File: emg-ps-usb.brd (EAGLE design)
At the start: 58.4 x 19.1 mm, 13 parts, among them U2 PHONE_JACK_MONO, X1 53047-04

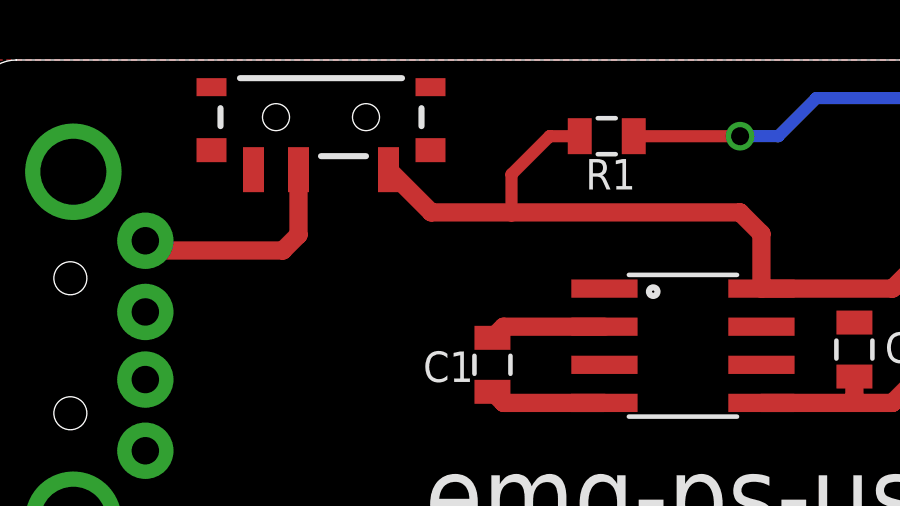
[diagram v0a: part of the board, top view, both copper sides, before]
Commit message: Cleaned up schematic and added a frame.
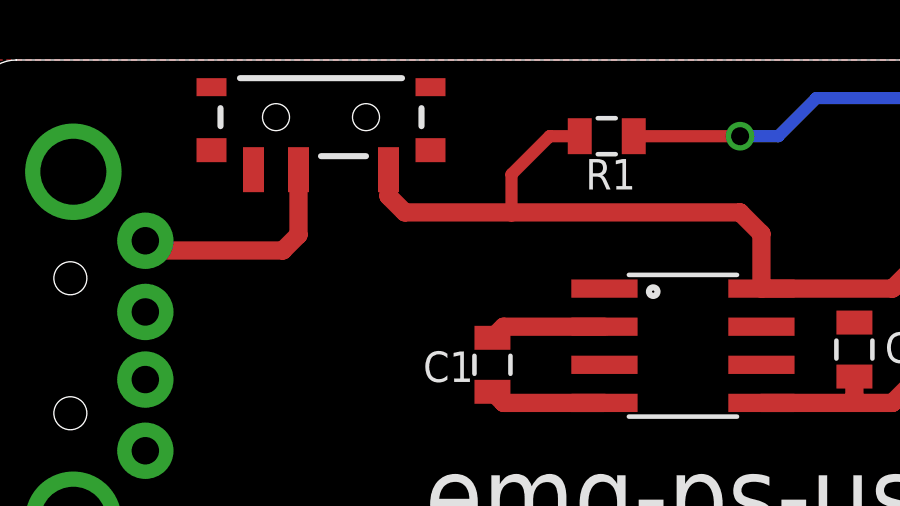
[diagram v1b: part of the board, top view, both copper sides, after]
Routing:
- net VBUS: track 33.2 -> 33.7 mm
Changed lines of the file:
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@@
 <wire x1="26.1112" y1="13.2588" x2="25.4" y2="13.97" width="0.6096" layer="1"/>
 <wire x1="25.4" y1="13.97" x2="17.78" y2="13.97" width="0.6096" layer="1"/>
-<wire x1="17.78" y1="13.97" x2="15.105" y2="13.97" width="0.6096" layer="1"/>
-<wire x1="15.105" y1="13.97" x2="13.68" y2="15.395" width="0.6096" layer="1"/>
 <wire x1="20.055" y1="16.51" x2="19.05" y2="16.51" width="0.4064" layer="1"/>
 <wire x1="19.05" y1="16.51" x2="17.78" y2="15.24" width="0.4064" layer="1"/>
 <wire x1="17.78" y1="15.24" x2="17.78" y2="13.97" width="0.4064" layer="1"/>
+<wire x1="13.68" y1="15.395" x2="13.68" y2="14.514" width="0.6096" layer="1"/>
+<wire x1="13.68" y1="14.514" x2="14.224" y2="13.97" width="0.6096" layer="1"/>
+<wire x1="14.224" y1="13.97" x2="17.78" y2="13.97" width="0.6096" layer="1"/>
 </signal>
 <signal name="N$3">

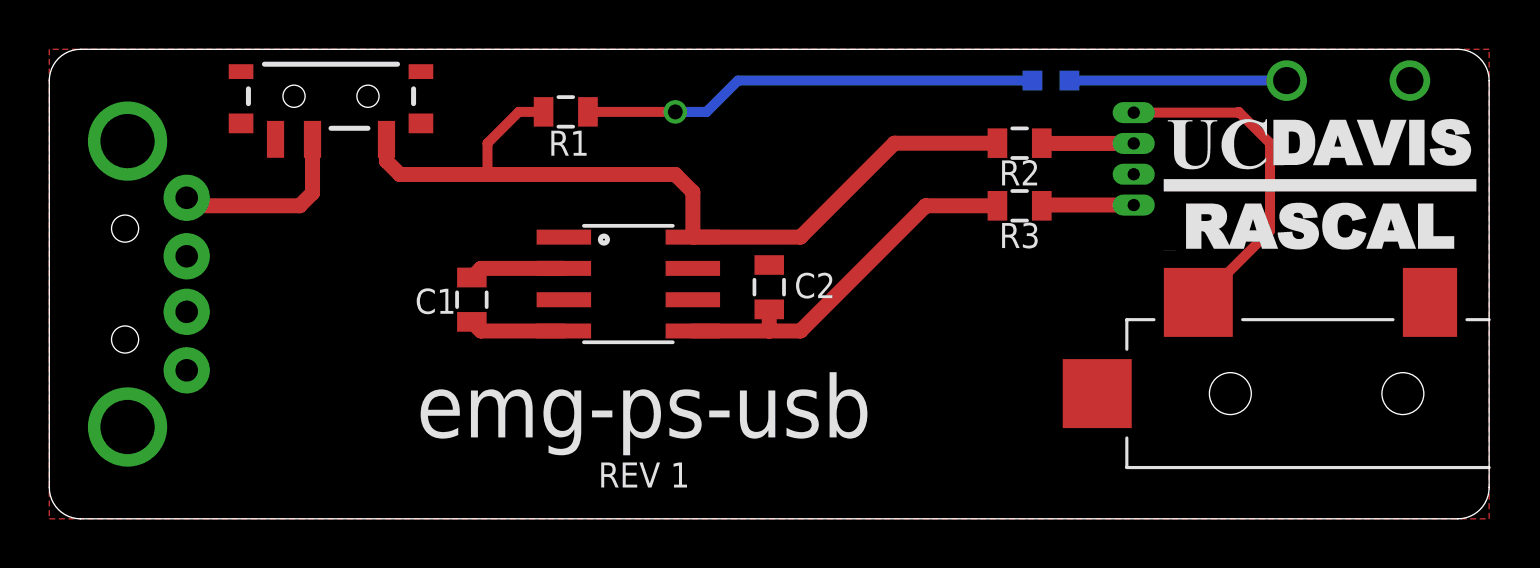
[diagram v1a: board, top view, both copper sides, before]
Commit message: Added labels to the EMG amp connector. Decreased size of component names.
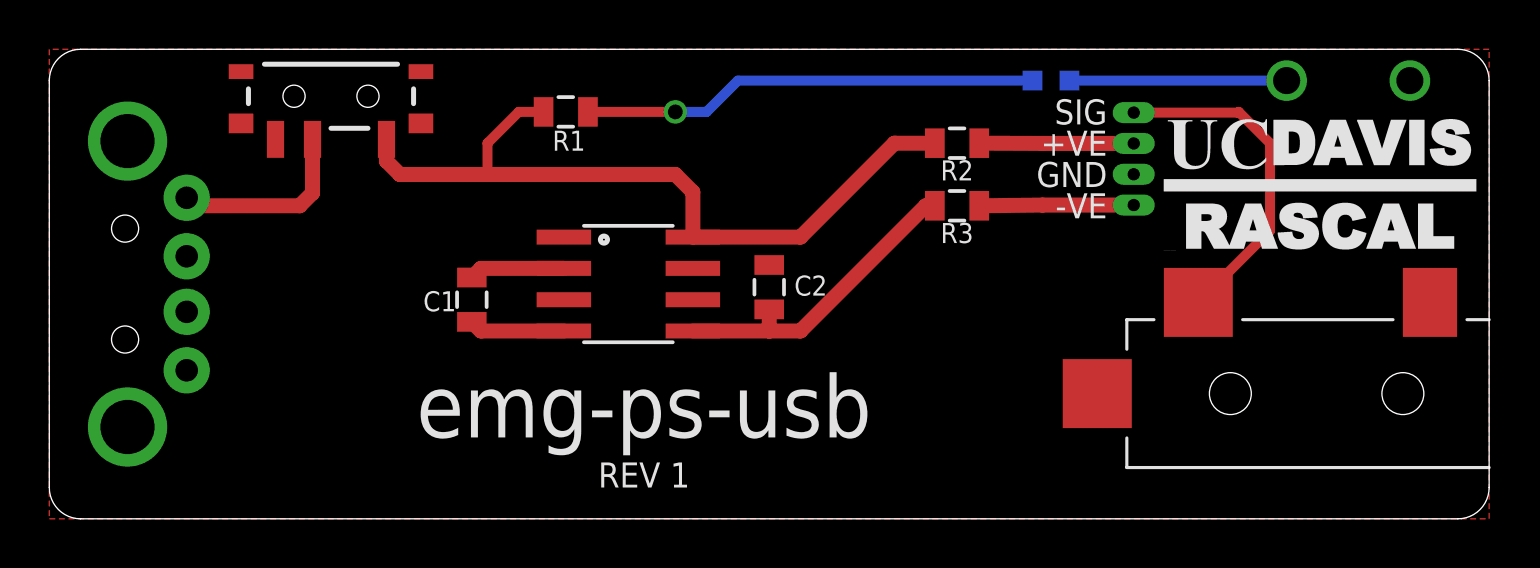
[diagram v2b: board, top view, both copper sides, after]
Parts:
- moved R2 2.54 mm to (36.8, 15.2)
- moved R3 2.54 mm to (36.8, 12.7)
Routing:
- net VBUS: track 33.7 -> 31.1 mm
- net N$4: track 15.3 -> 12.8 mm
- net +VE: track 3.73 -> 6.27 mm
- net -VE: track 3.74 -> 6.27 mm
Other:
- board text added: "+VE"
- board text added: "-VE"
- board text added: "GND"
- board text added: "SIG"
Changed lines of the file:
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@@
 <text x="24.13" y="3.302" size="2.54" layer="21" font="vector" ratio="13" rot="SR0" align="bottom-center">emg-ps-usb</text>
 <text x="24.13" y="1.27" size="1.016" layer="21" font="vector" ratio="10" align="bottom-center">REV 1</text>
+<text x="42.926" y="16.51" size="1.016" layer="21" font="vector" ratio="10" align="center-right">SIG</text>
+<text x="42.926" y="15.24" size="1.016" layer="21" font="vector" ratio="10" align="center-right">+VE</text>
+<text x="42.926" y="13.97" size="1.016" layer="21" font="vector" ratio="10" align="center-right">GND</text>
+<text x="42.926" y="12.7" size="1.016" layer="21" font="vector" ratio="10" align="center-right">-VE</text>
 </plain>
 <attributes>
@@
 <element name="U$2" library="eagle-lib" package="SOIC8" value="ADM660ARZ" x="23.495" y="9.525" smashed="yes" rot="R270"/>
 <element name="R1" library="SparkFun-Resistors" package="0805" value="1k" x="20.955" y="16.51" smashed="yes" rot="R180">
-<attribute name="NAME" x="21.082" y="15.748" size="1.016" layer="25" font="vector" align="top-center"/>
+<attribute name="NAME" x="21.082" y="15.748" size="0.8128" layer="25" font="vector" align="top-center"/>
 </element>
 <element name="D1" library="SparkFun-LED" package="LED-0603" value="RED" x="40.64" y="17.78" smashed="yes" rot="MR90">
@@
 </element>
 <element name="C1" library="SparkFun-Capacitors" package="0805" value="10uF" x="17.145" y="8.89" smashed="yes" rot="R270">
-<attribute name="NAME" x="16.51" y="8.8265" size="1.016" layer="25" font="vector" align="center-right"/>
+<attribute name="NAME" x="16.51" y="8.8265" size="0.8128" layer="25" font="vector" align="center-right"/>
 </element>
 <element name="C2" library="SparkFun-Capacitors" package="0805" value="10uF" x="29.21" y="9.398" smashed="yes" rot="R90">
-<attribute name="NAME" x="30.226" y="9.4615" size="1.016" layer="25" font="vector" align="center-left"/>
-</element>
-<element name="R2" library="SparkFun-Resistors" package="0805" value="100" x="39.37" y="15.24" smashed="yes">
-<attribute name="NAME" x="39.37" y="14.5415" size="1.016" layer="25" font="vector" align="top-center"/>
-</element>
-<element name="R3" library="SparkFun-Resistors" package="0805" value="100" x="39.37" y="12.7" smashed="yes">
-<attribute name="NAME" x="39.37" y="12.0015" size="1.016" layer="25" font="vector" align="top-center"/>
+<attribute name="NAME" x="30.226" y="9.4615" size="0.8128" layer="25" font="vector" align="center-left"/>
+</element>
+<element name="R2" library="SparkFun-Resistors" package="0805" value="100" x="36.83" y="15.24" smashed="yes">
+<attribute name="NAME" x="36.83" y="14.5415" size="0.8128" layer="25" font="vector" align="top-center"/>
+</element>
+<element name="R3" library="SparkFun-Resistors" package="0805" value="100" x="36.83" y="12.7" smashed="yes">
+<attribute name="NAME" x="36.83" y="12.0015" size="0.8128" layer="25" font="vector" align="top-center"/>
 </element>
 <element name="X1" library="con-molex" package="53047-04" value="53047-04" x="44.45" y="14.605" smashed="yes" rot="MR270">
@@
 <contactref element="U$2" pad="8"/>
 <contactref element="R2" pad="1"/>
-<wire x1="38.47" y1="15.24" x2="34.29" y2="15.24" width="0.6096" layer="1"/>
+<wire x1="35.93" y1="15.24" x2="34.29" y2="15.24" width="0.6096" layer="1"/>
 <wire x1="34.29" y1="15.24" x2="30.48" y2="11.43" width="0.6096" layer="1"/>
 <wire x1="30.48" y1="11.43" x2="26.1112" y2="11.43" width="0.6096" layer="1"/>
@@
 <contactref element="R3" pad="1"/>
 <contactref element="C2" pad="1"/>
-<wire x1="38.47" y1="12.7" x2="35.56" y2="12.7" width="0.6096" layer="1"/>
+<wire x1="35.93" y1="12.7" x2="35.56" y2="12.7" width="0.6096" layer="1"/>
 <wire x1="35.56" y1="12.7" x2="30.48" y2="7.62" width="0.6096" layer="1"/>
 <wire x1="30.48" y1="7.62" x2="29.21" y2="7.62" width="0.6096" layer="1"/>
@@
 <contactref element="X1" pad="3"/>
 <wire x1="44" y1="15.23" x2="40.28" y2="15.23" width="0.6096" layer="1"/>
-<wire x1="40.28" y1="15.23" x2="40.27" y2="15.24" width="0.6096" layer="1"/>
+<wire x1="40.28" y1="15.23" x2="37.73" y2="15.24" width="0.6096" layer="1"/>
 </signal>
 <signal name="-VE">
@@
 <contactref element="X1" pad="1"/>
 <wire x1="44" y1="12.73" x2="40.3" y2="12.73" width="0.6096" layer="1"/>
-<wire x1="40.3" y1="12.73" x2="40.27" y2="12.7" width="0.6096" layer="1"/>
+<wire x1="40.3" y1="12.73" x2="37.73" y2="12.7" width="0.6096" layer="1"/>
 </signal>
 <signal name="N$5">

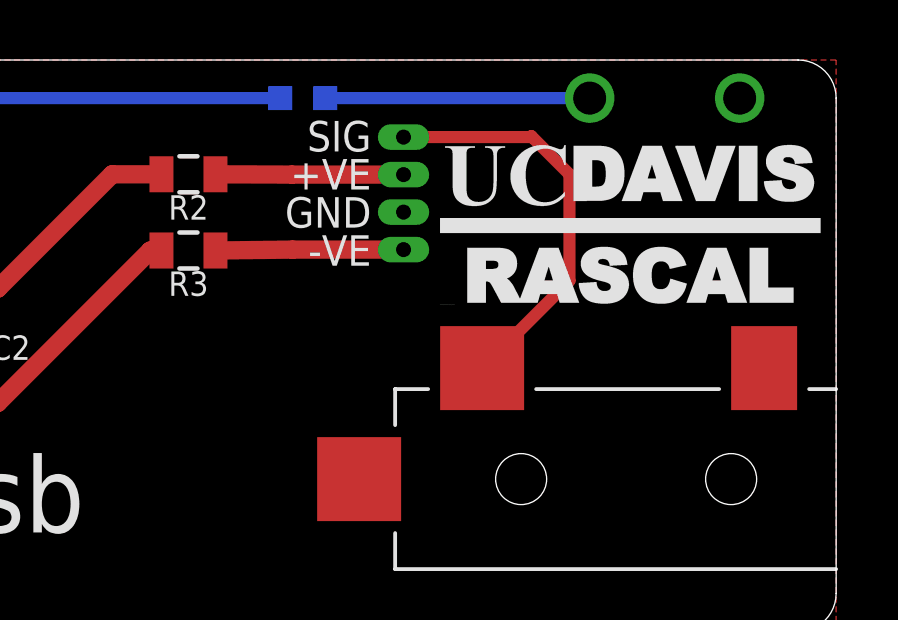
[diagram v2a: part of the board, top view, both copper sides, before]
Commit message: Now using EMG amp outline and UCDAVIS|RASCAL logo from ucdrascal-eagle-lib.
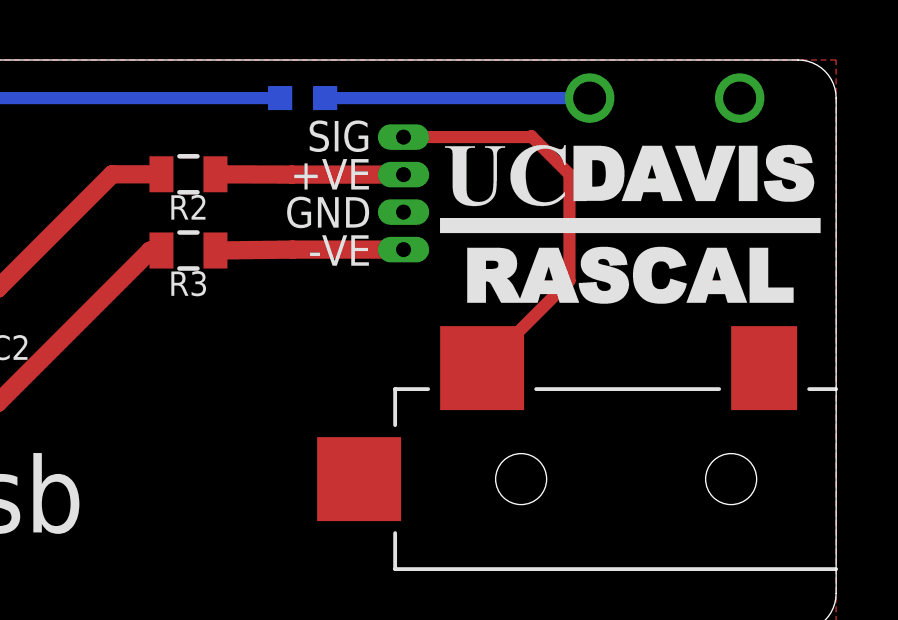
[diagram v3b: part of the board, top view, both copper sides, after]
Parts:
- added U$3: EMG_AMP_OUTLINE-Y03ENDS, ucdrascal-eagle-lib:EMG_Y03_OUTLINEENDS
- U$1: value UCDAVIS-RASCAL_LOGO -> UCDAVIS-RASCAL_LOGO-2LINE; device eagle-lib:UCDAVIS-RASCAL_LOGO -> ucdrascal-eagle-lib:UCDAVIS-RASCAL_LOGO
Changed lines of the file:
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@@
 <layer number="27" name="tValues" color="7" fill="1" visible="yes" active="yes"/>
 <layer number="28" name="bValues" color="7" fill="1" visible="yes" active="yes"/>
-<layer number="29" name="tStop" color="7" fill="3" visible="no" active="yes"/>
-<layer number="30" name="bStop" color="7" fill="6" visible="no" active="yes"/>
+<layer number="29" name="tStop" color="7" fill="3" visible="yes" active="yes"/>
+<layer number="30" name="bStop" color="7" fill="6" visible="yes" active="yes"/>
 <layer number="31" name="tCream" color="7" fill="4" visible="no" active="yes"/>
 <layer number="32" name="bCream" color="7" fill="5" visible="no" active="yes"/>
@@
 <layer number="35" name="tGlue" color="7" fill="4" visible="no" active="yes"/>
 <layer number="36" name="bGlue" color="7" fill="5" visible="no" active="yes"/>
-<layer number="37" name="tTest" color="7" fill="1" visible="no" active="yes"/>
-<layer number="38" name="bTest" color="7" fill="1" visible="no" active="yes"/>
+<layer number="37" name="tTest" color="7" fill="1" visible="yes" active="yes"/>
+<layer number="38" name="bTest" color="7" fill="1" visible="yes" active="yes"/>
 <layer number="39" name="tKeepout" color="4" fill="11" visible="yes" active="yes"/>
 <layer number="40" name="bKeepout" color="1" fill="11" visible="yes" active="yes"/>
@@
 <layer number="42" name="bRestrict" color="1" fill="10" visible="yes" active="yes"/>
 <layer number="43" name="vRestrict" color="2" fill="10" visible="yes" active="yes"/>
-<layer number="44" name="Drills" color="7" fill="1" visible="no" active="yes"/>
+<layer number="44" name="Drills" color="7" fill="1" visible="yes" active="yes"/>
 <layer number="45" name="Holes" color="7" fill="1" visible="yes" active="yes"/>
-<layer number="46" name="Milling" color="3" fill="1" visible="no" active="yes"/>
-<layer number="47" name="Measures" color="7" fill="1" visible="no" active="yes"/>
+<layer number="46" name="Milling" color="3" fill="1" visible="yes" active="yes"/>
+<layer number="47" name="Measures" color="7" fill="1" visible="yes" active="yes"/>
 <layer number="48" name="Document" color="7" fill="1" visible="yes" active="yes"/>
 <layer number="49" name="Reference" color="7" fill="1" visible="yes" active="yes"/>
@@
 <board>
 <plain>
-<wire x1="45.72" y1="9.271" x2="45.72" y2="0.381" width="0.4064" layer="22"/>
-<wire x1="17.272" y1="18.796" x2="17.272" y2="0.254" width="0.4064" layer="22" curve="180"/>
-<wire x1="33.02" y1="18.796" x2="42.545" y2="9.271" width="0.4064" layer="22" curve="-90"/>
-<wire x1="42.545" y1="9.271" x2="45.72" y2="9.271" width="0.4064" layer="22"/>
 <wire x1="57.15" y1="19.05" x2="1.27" y2="19.05" width="0" layer="20"/>
 <wire x1="1.27" y1="19.05" x2="0" y2="17.78" width="0" layer="20" curve="90"/>
@@
 <element name="JP1" library="SparkFun-Connectors" package="USB-A-H" value="USB-A-H" x="3.175" y="9.525" smashed="yes" rot="MR180"/>
 <element name="U2" library="eagle-lib" package="MJ-3523-SMT" value="PHONE_JACK_MONO" x="58.42" y="5.08" smashed="yes"/>
-<element name="U$1" library="eagle-lib" package="UCDAVIS-RASCAL_LOGO" value="UCDAVIS-RASCAL_LOGO" x="45.212" y="10.922"/>
+<element name="U$1" library="ucdrascal-eagle-lib" package="UCDAVIS-RASCAL_LOGO" value="UCDAVIS-RASCAL_LOGO-2LINE" x="45.212" y="10.922"/>
+<element name="U$3" library="ucdrascal-eagle-lib" package="EMG_Y03_OUTLINEENDS" value="EMG_AMP_OUTLINE-Y03ENDS" x="44.958" y="-0.254" rot="MR0"/>
 </elements>
 <signals>

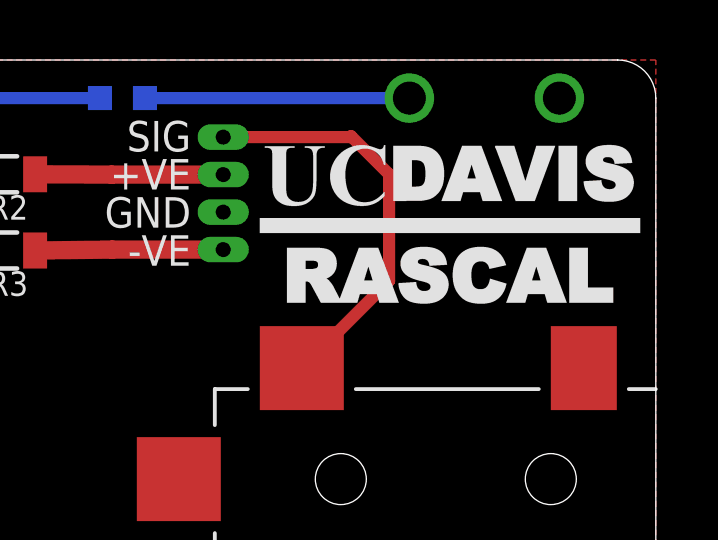
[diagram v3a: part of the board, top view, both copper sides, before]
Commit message: Refreshed library parts (UCDAVIS|RASCAL logo).
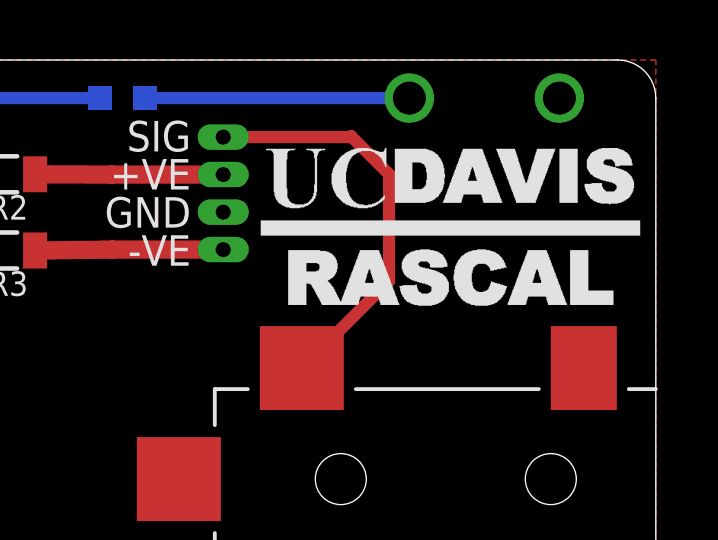
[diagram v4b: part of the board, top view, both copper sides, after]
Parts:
- moved U$1 6.84 mm to (51.6, 13.5)
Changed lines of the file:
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@@
 <element name="JP1" library="SparkFun-Connectors" package="USB-A-H" value="USB-A-H" x="3.175" y="9.525" smashed="yes" rot="MR180"/>
 <element name="U2" library="eagle-lib" package="MJ-3523-SMT" value="PHONE_JACK_MONO" x="58.42" y="5.08" smashed="yes"/>
-<element name="U$1" library="ucdrascal-eagle-lib" package="UCDAVIS-RASCAL_LOGO" value="UCDAVIS-RASCAL_LOGO-2LINE" x="45.212" y="10.922"/>
+<element name="U$1" library="ucdrascal-eagle-lib" package="UCDAVIS-RASCAL_LOGO" value="UCDAVIS-RASCAL_LOGO-2LINE" x="51.562" y="13.462"/>
 <element name="U$3" library="ucdrascal-eagle-lib" package="EMG_Y03_OUTLINEENDS" value="EMG_AMP_OUTLINE-Y03ENDS" x="44.958" y="-0.254" rot="MR0"/>
 </elements>
